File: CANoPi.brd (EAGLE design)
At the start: 65 x 30 mm, 28 parts, among them IC1 ISO7242, IC2 B0505LS, U1 MCP2515(MCP2510)SS, U2 DS1307Z, U3 MCP2551, Y1 16M, Y2 32768

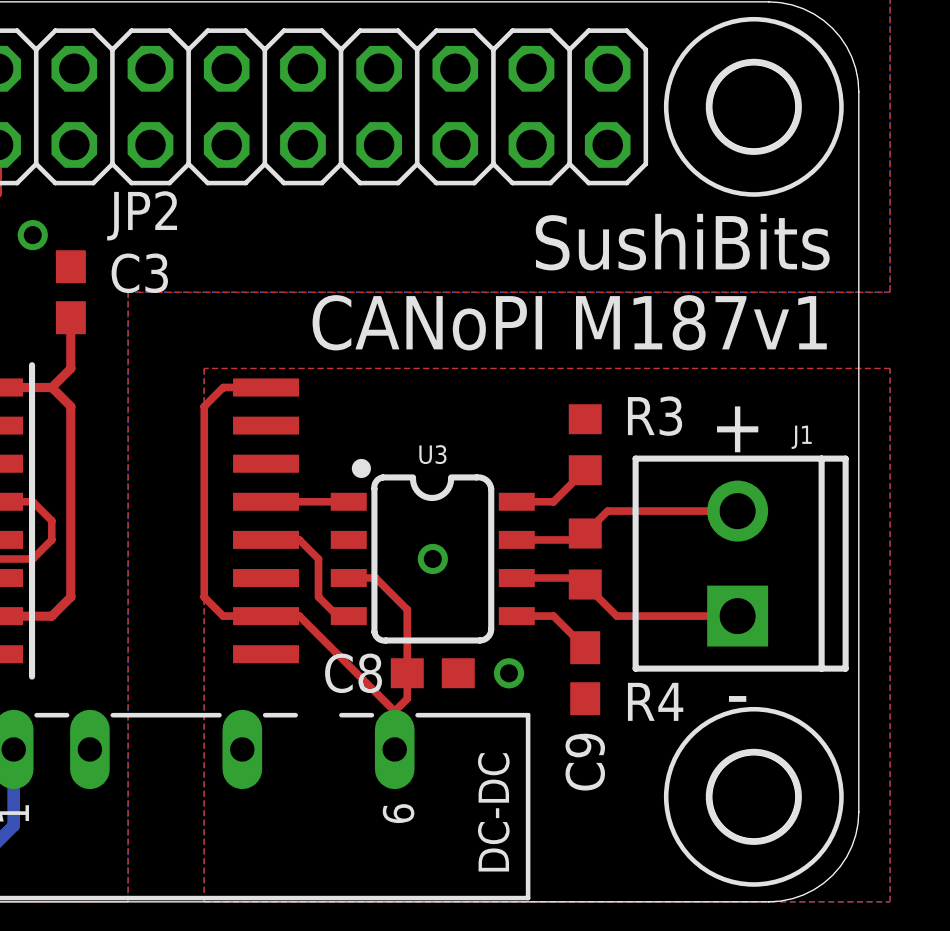
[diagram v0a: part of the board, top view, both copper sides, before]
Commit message: Fixed the CAN GND pin issue
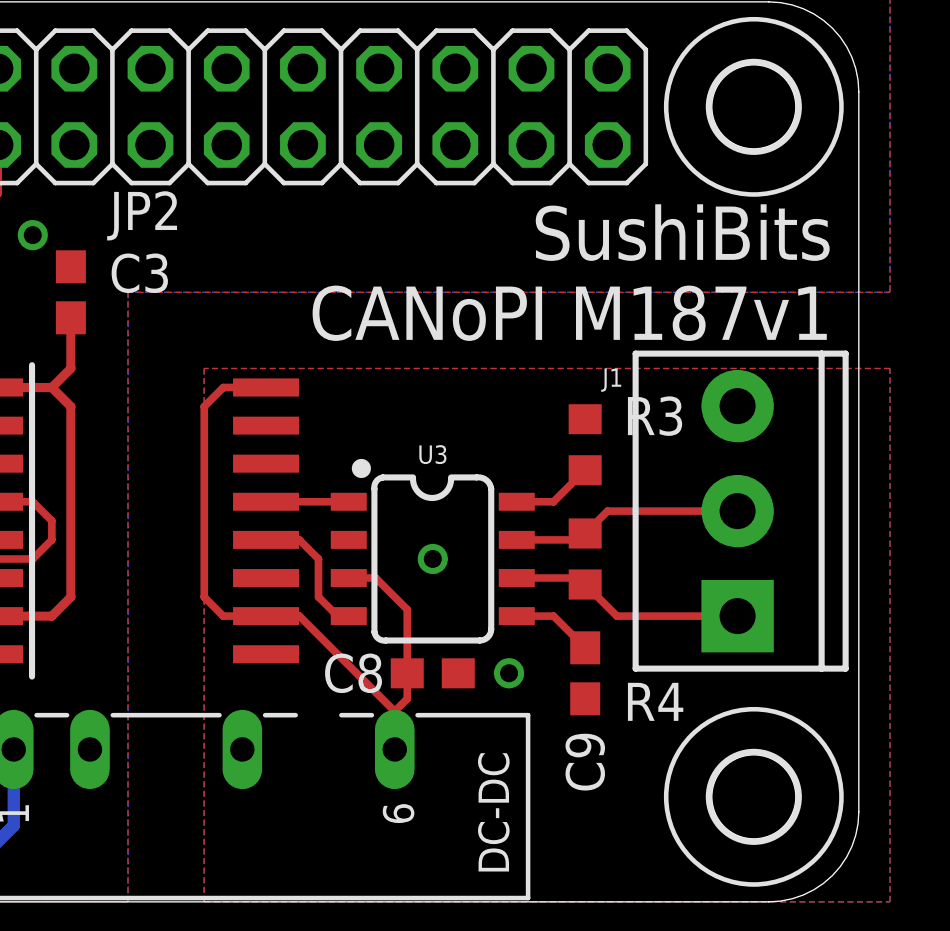
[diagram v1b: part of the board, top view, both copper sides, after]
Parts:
- J1: device SparkFun-Connectors:SCREWTERMINAL-3.5MM-2 -> SparkFun-Connectors:SCREWTERMINAL-3.5MM-3
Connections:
- net GND-ISO: now also J1.3
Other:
- board text added: "CANH"
- board text added: "CANL"
- board text removed: "+"
- board text removed: "-"
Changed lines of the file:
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@@
 <wire x1="65" y1="27" x2="65" y2="3" width="0" layer="20"/>
 <wire x1="62" y1="0" x2="3" y2="0" width="0" layer="20"/>
-<text x="64.135" y="18.415" size="1.778" layer="21" align="bottom-right">SushiBits
+<text x="64.135" y="20.955" size="1.778" layer="21" align="center-right">SushiBits
 CANoPI M187v1</text>
 <text x="26.67" y="9.525" size="1.778" layer="21" rot="R270" align="center-right">TX</text>
 <text x="29.21" y="9.525" size="1.778" layer="21" rot="R270" align="center-right">RX</text>
 <text x="24.13" y="9.525" size="1.778" layer="21" rot="R270" align="center-right">GND</text>
-<text x="13.335" y="16.51" size="2.54" layer="22" rot="MR0" align="center-right">SushiBits CANoPI M187v1</text>
-<text x="59.055" y="12.7" size="1.778" layer="22" rot="MR0" align="center-left">(c) 2017 Max Chan
+<text x="50.165" y="20.955" size="1.778" layer="22" rot="MR0" align="center-left">(c) 2017 Max Chan
 OSHW. 3-BSDL</text>
-<text x="60.96" y="15.875" size="1.778" layer="21" align="center">+</text>
-<text x="60.96" y="6.985" size="1.778" layer="21" align="center">-</text>
+<text x="58.42" y="16.51" size="1.778" layer="22" rot="MR0" align="center-left">GND</text>
+<text x="58.42" y="13.0175" size="1.778" layer="22" rot="MR0" align="center-left">CANH</text>
+<text x="58.42" y="9.525" size="1.778" layer="22" rot="MR0" align="center-left">CANL</text>
 </plain>
 <attributes>
@@
 <attribute name="VALUE" x="47.117" y="2.54" size="1.27" layer="27" ratio="10" rot="R180"/>
 </element>
-<element name="J1" library="SparkFun-Connectors" package="SCREWTERMINAL-3.5MM-2" value="" x="60.96" y="9.525" smashed="yes" rot="R90">
-<attribute name="NAME" x="63.5" y="15.875" size="0.6096" layer="25" font="vector" ratio="20" rot="R180"/>
-<attribute name="PROD_ID" value="CONN-08399" x="60.96" y="9.525" size="1.778" layer="27" rot="R90" display="off"/>
+<element name="J1" library="SparkFun-Connectors" package="SCREWTERMINAL-3.5MM-3" value="" x="60.96" y="9.525" smashed="yes" rot="R90">
+<attribute name="NAME" x="57.15" y="17.78" size="0.6096" layer="25" font="vector" ratio="20" rot="R180"/>
+<attribute name="PROD_ID" value="CONN-08288" x="60.96" y="9.525" size="1.778" layer="27" rot="R90" display="off"/>
+<attribute name="SF_ID" value="PRT-08235" x="60.96" y="9.525" size="1.778" layer="27" rot="R90" display="off"/>
 <attribute name="VALUE" x="59.69" y="8.255" size="0.6096" layer="27" font="vector" ratio="20" rot="R90"/>
 </element>
@@
 <vertex x="43.18" y="17.78"/>
 </polygon>
+<contactref element="J1" pad="3"/>
 </signal>
 <signal name="VCC">
